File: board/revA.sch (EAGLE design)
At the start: 28 parts, among them IC1 LM2931, U1 LDK120DM33R

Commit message: Updating values
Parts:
- added C4: 1uF 5v, rcl:C-EUC0603
- added R11: 10k, rcl:R-EU_R0603
- D1, D2, D3, D4: value (none) -> 80V
- R10, R7, R8, R9: value (none) -> 470R
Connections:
- new net N$1: C4.1, R11.2
- new net NRST: C4.2, MCURESET.NRST
- net +3V3: now also MCUAN_POWER.VBAT, MCUAN_POWER.VDDA, MCUPOWER.VDD_1, MCUPOWER.VDD_2, MCUPOWER.VDD_3, MCURESET.BOOT0, R11.1
- net GND: now also MCUAN_POWER.VSSA, MCUPOWER.VSS_1, MCUPOWER.VSS_2, MCUPOWER.VSS_3
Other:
- note added: "Fake injectors for ECU to see"
- note added: "Flyback diodes"
- note removed: "Flywheel diodes"
- moved on the sheet: R10, R7, R8, R9

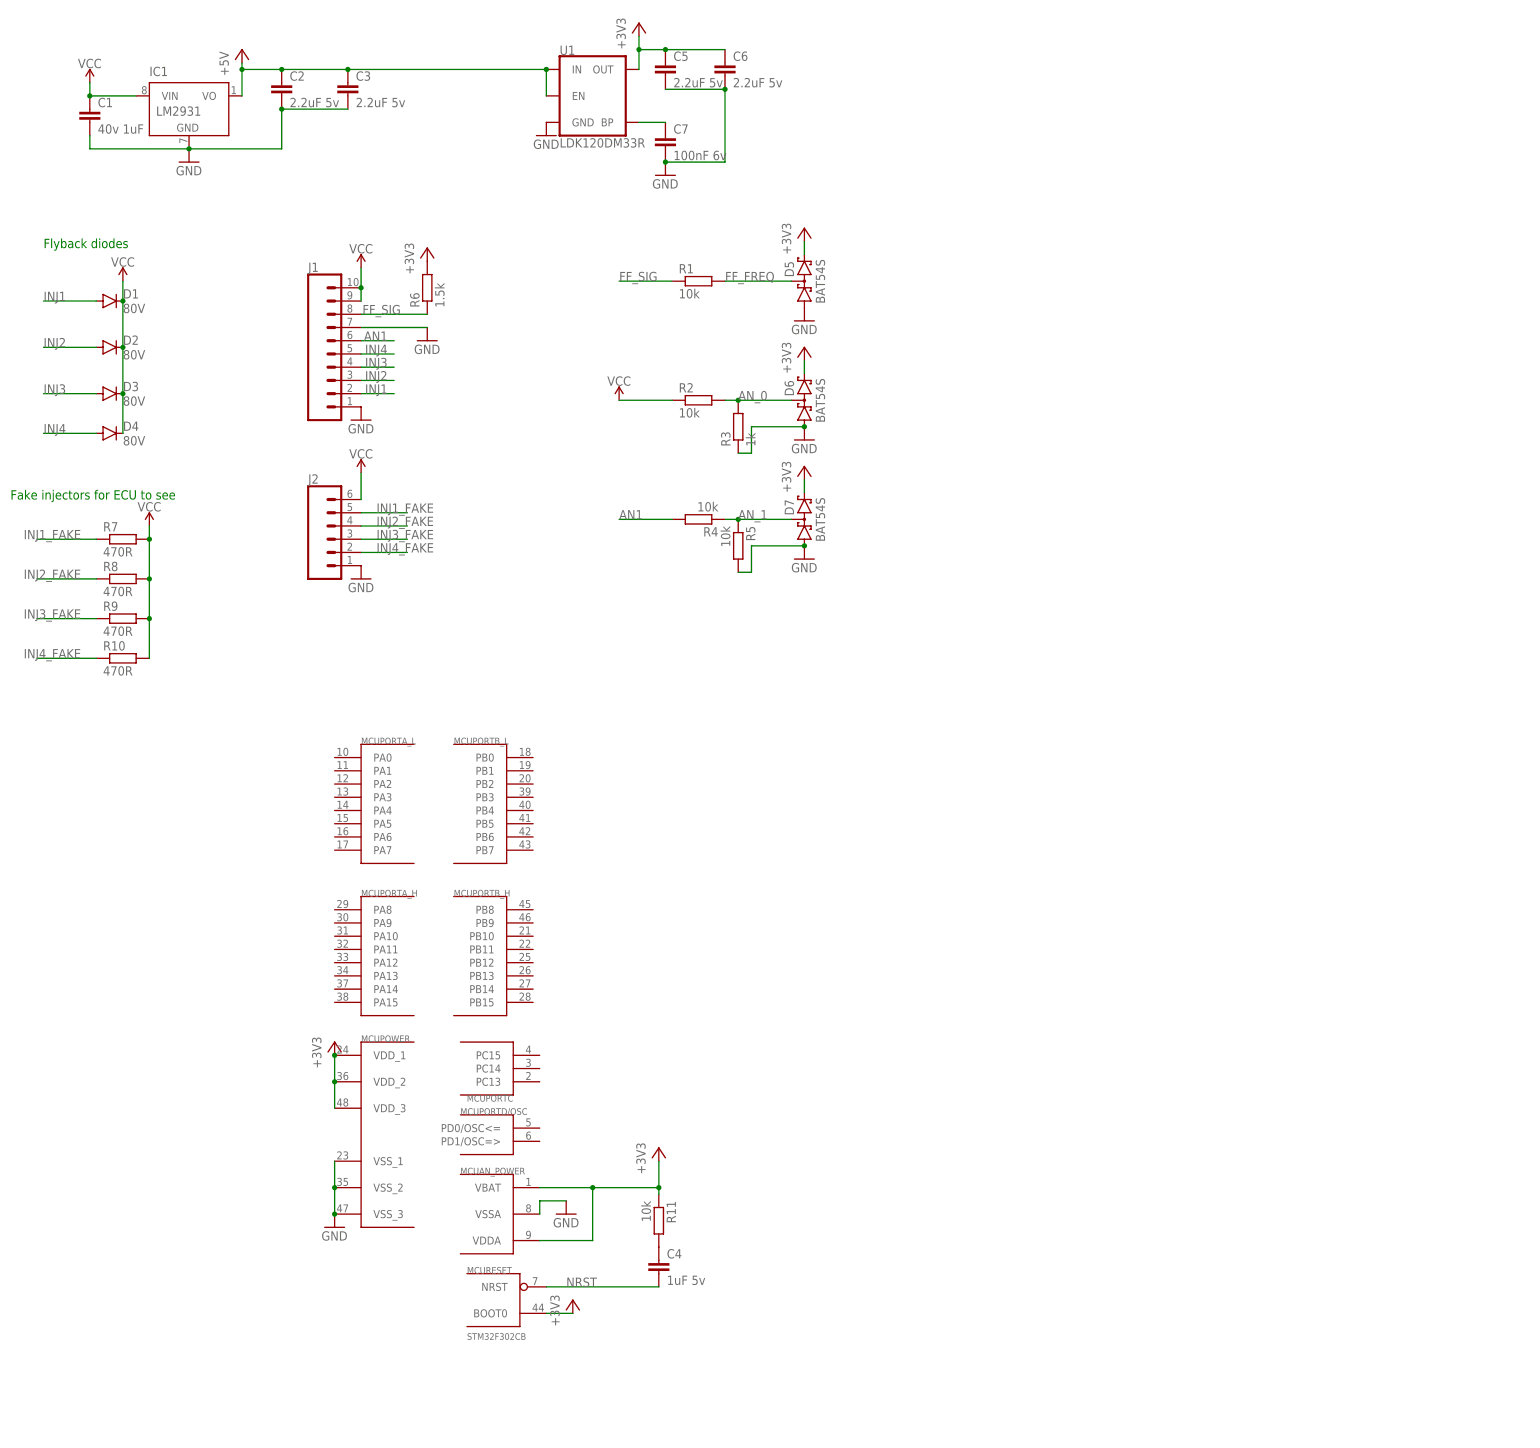
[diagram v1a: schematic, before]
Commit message: Some routing, adding mosfets
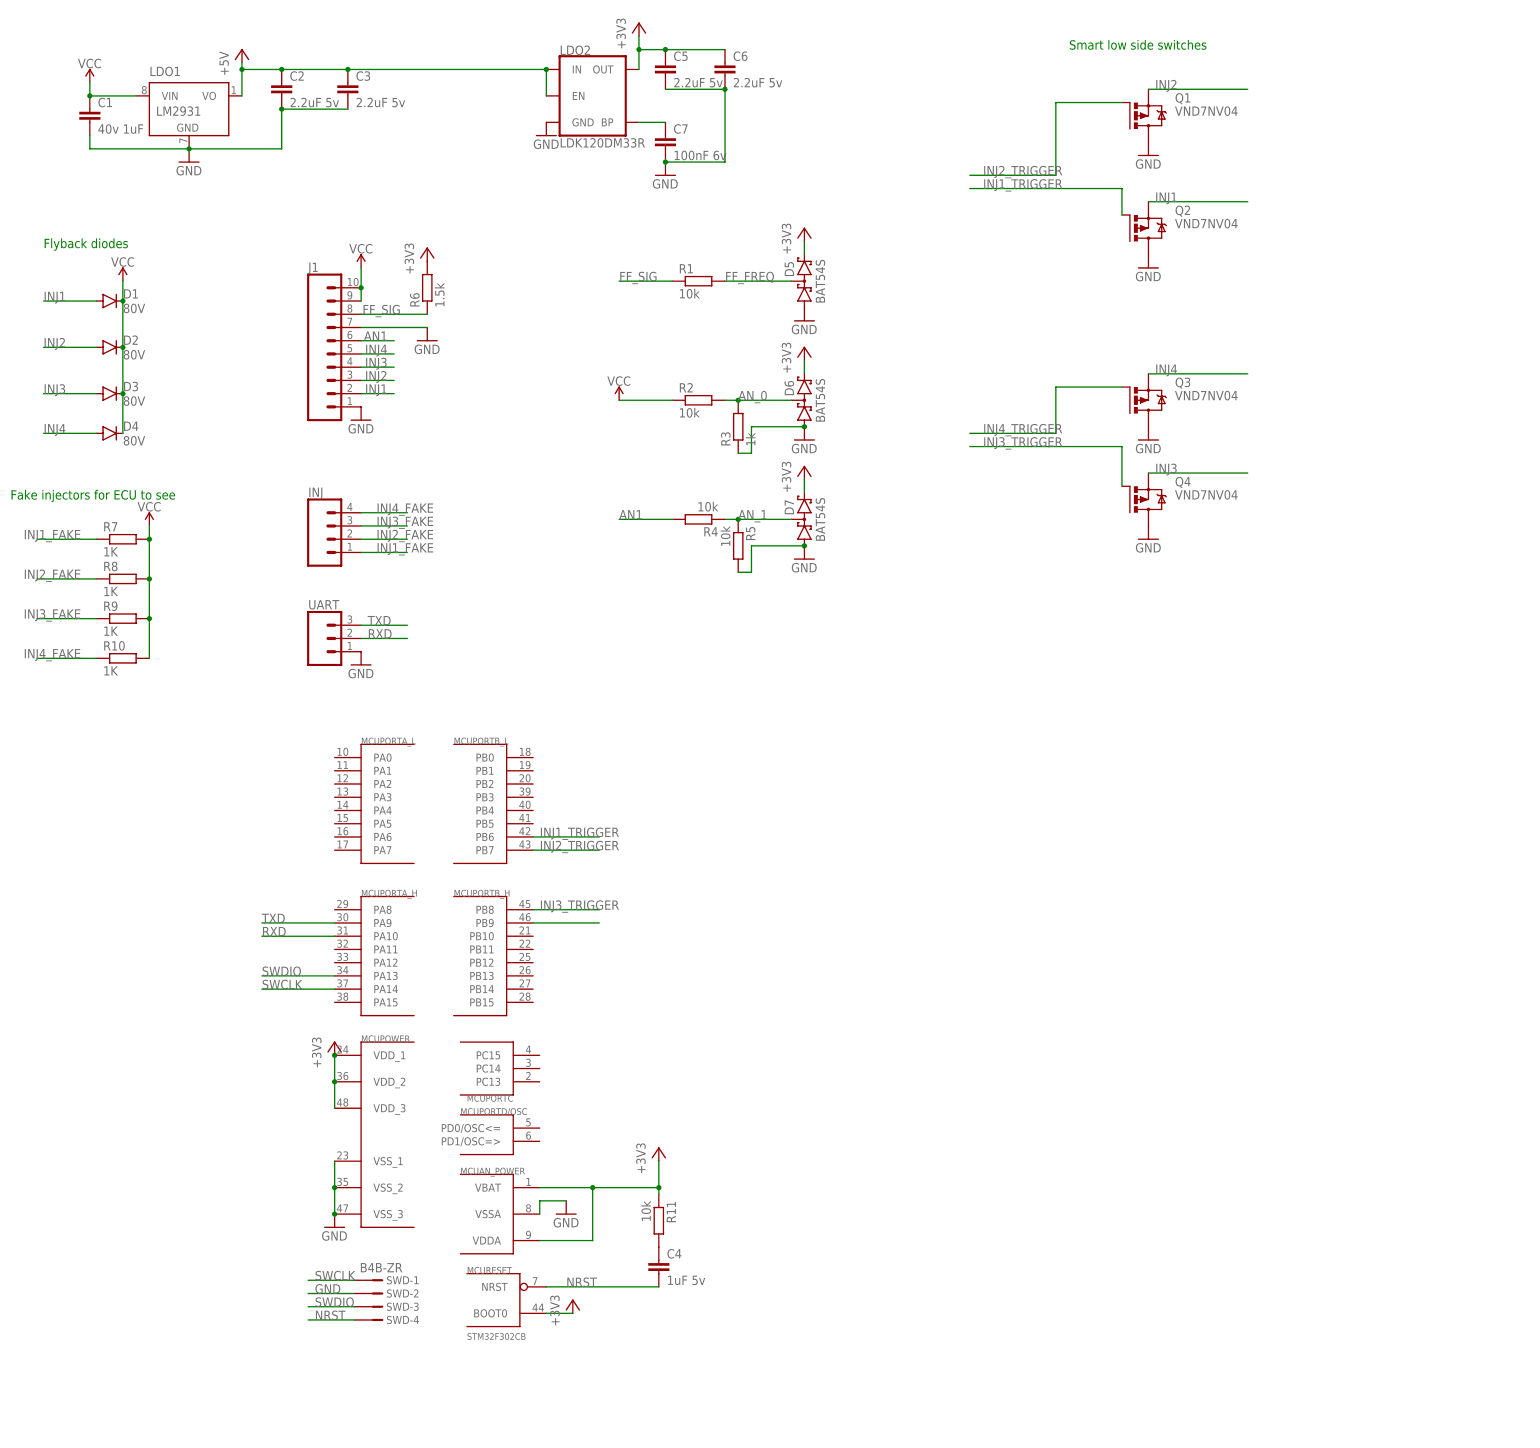
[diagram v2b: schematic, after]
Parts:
- removed J2: (no value), SparkFun-Connectors:CONN_06SILK_FEMALE_PTH
- added INJ: (no value), SparkFun-Connectors:CONN_04
- added Q1, Q2, Q3, Q4: VND7NV04, transistor-power:IRFR5305
- added SWD: B4B-ZR, con-jst:B4B-ZR
- added UART: (no value), SparkFun-Connectors:CONN_03
- R10, R7, R8, R9: value 470R -> 1K; device rcl:R-EU_0414/15 -> rcl:R-EU_0207/7
- renumbered IC1 to LDO1, U1 to LDO2
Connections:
- new net INJ1_TRIGGER: MCUPORTB_L.PB6, Q2.G
- new net INJ2_TRIGGER: MCUPORTB_L.PB7, Q1.G
- new net INJ3_TRIGGER: MCUPORTB_H.PB8, Q4.G
- new net INJ4_TRIGGER: MCUPORTB_H.PB9, Q3.G
- new net RXD: MCUPORTA_H.PA10, UART.2
- new net SWCLK: MCUPORTA_H.PA14, SWD-1.1
- new net SWDIO: MCUPORTA_H.PA13, SWD-3.1
- new net TXD: MCUPORTA_H.PA9, UART.3
- net GND: now also Q1.D, Q2.D, Q3.D, Q4.D, SWD-2.1, UART.1; no longer J2.1
- net INJ1: now also Q2.S
- net INJ1_FAKE: now also INJ.1; no longer J2.5
- net INJ2: now also Q1.S
- net INJ2_FAKE: now also INJ.2; no longer J2.4
- net INJ3: now also Q4.S
- net INJ3_FAKE: now also INJ.3; no longer J2.3
- net INJ4: now also Q3.S
- net INJ4_FAKE: now also INJ.4; no longer J2.2
- net NRST: now also SWD-4.1
- net VCC: no longer J2.6
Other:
- note added: "Smart low side switches"

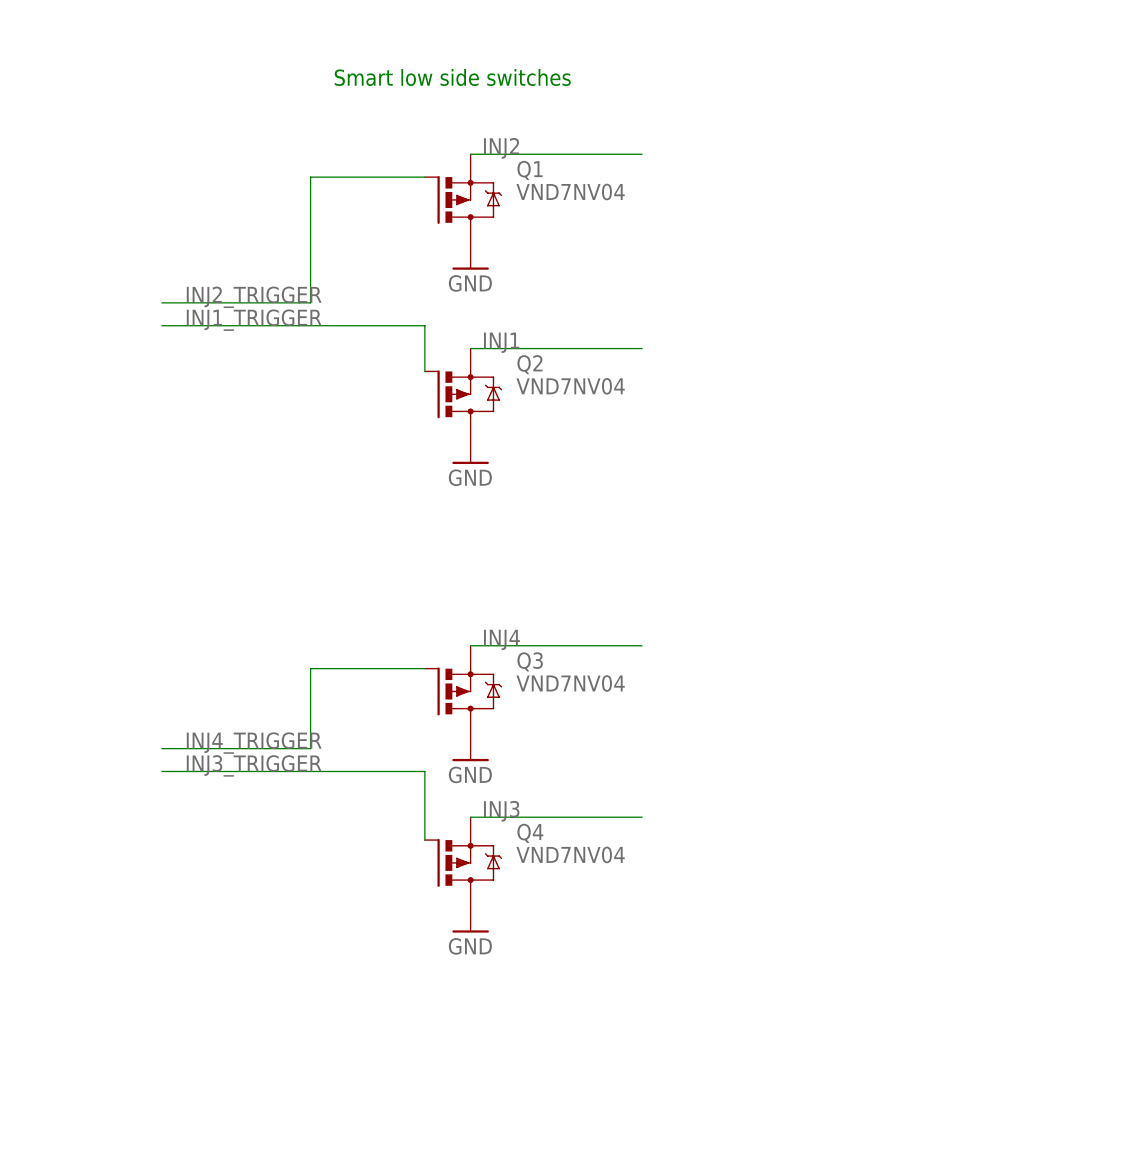
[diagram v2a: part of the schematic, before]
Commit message: Adding buffer for mosfets
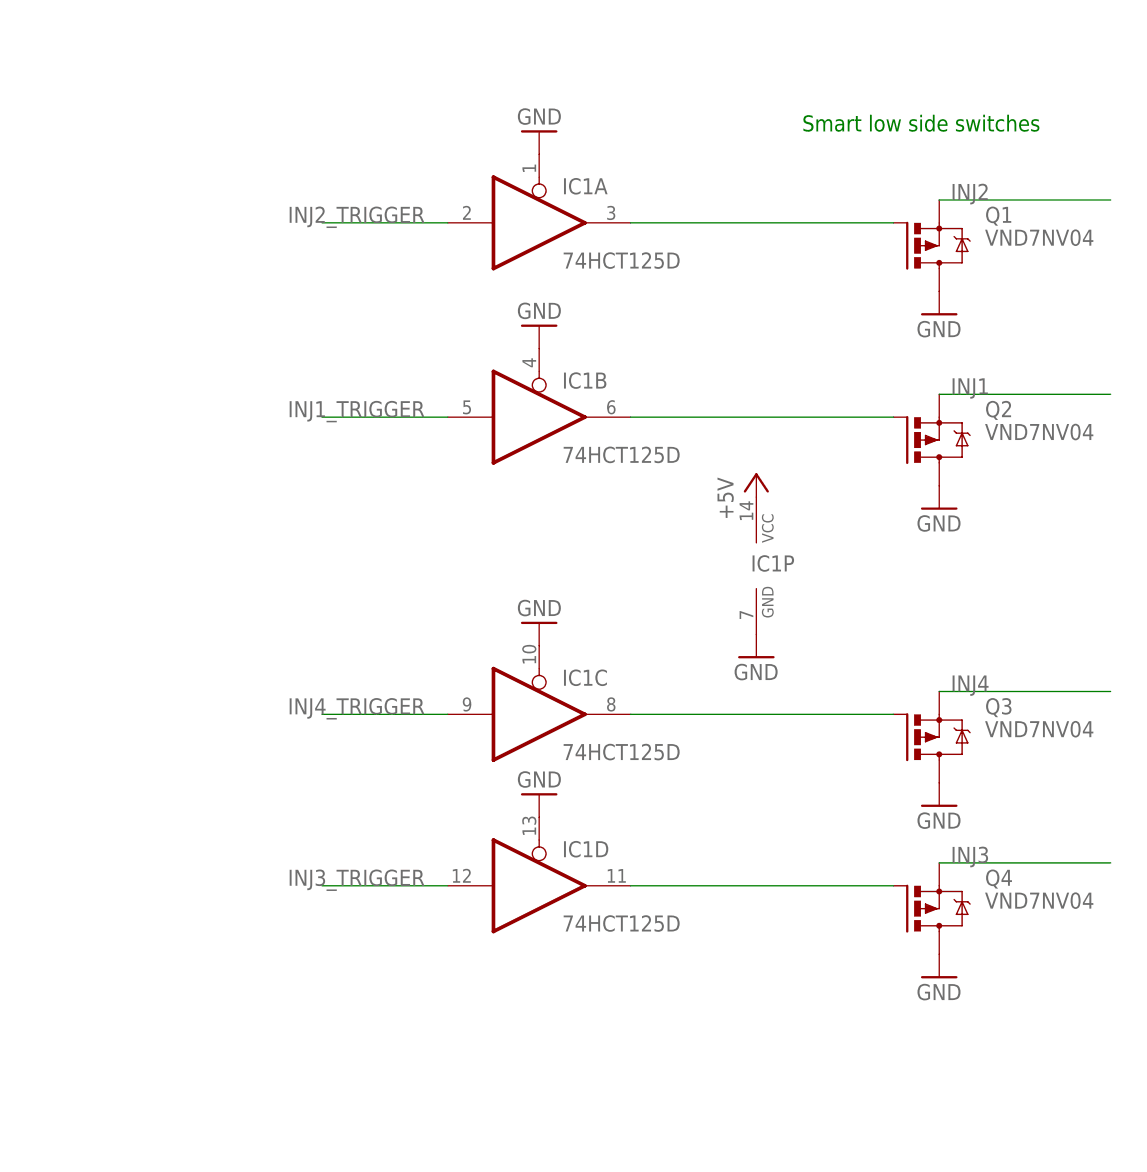
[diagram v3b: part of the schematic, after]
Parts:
- added IC1: 74HCT125D, 74xx-eu:74HCT125D
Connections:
- new net N$10: IC1C.O, Q3.G
- new net N$7: IC1B.O, Q2.G
- new net N$8: IC1A.O, Q1.G
- new net N$9: IC1D.O, Q4.G
- net +5V: now also IC1P.VCC
- net GND: now also IC1A.OE, IC1B.OE, IC1C.OE, IC1D.OE, IC1P.GND
- net INJ1_TRIGGER: now also IC1B.I; no longer Q2.G
- net INJ2_TRIGGER: now also IC1A.I; no longer Q1.G
- net INJ3_TRIGGER: now also IC1D.I; no longer Q4.G
- net INJ4_TRIGGER: now also IC1C.I; no longer Q3.G
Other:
- moved on the sheet: Q1, Q2, Q3, Q4
